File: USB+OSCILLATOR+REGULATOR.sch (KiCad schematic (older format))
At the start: 65 parts, among them J201 CONN_01X02, J202 USB_A, U201 MIC2005A-2, U202 74xx125, U203 93LCxxB_sot-23-6, U204 MIC5355/6-xYMME, U205 FT2232H

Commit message: Minor fixes and the gitignore was removed
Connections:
- net +5V: no longer R201.1, U201.3 (EN)
- net Vext_filtered: now also R201.1, U201.3 (EN)
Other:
- moved on the sheet: R201

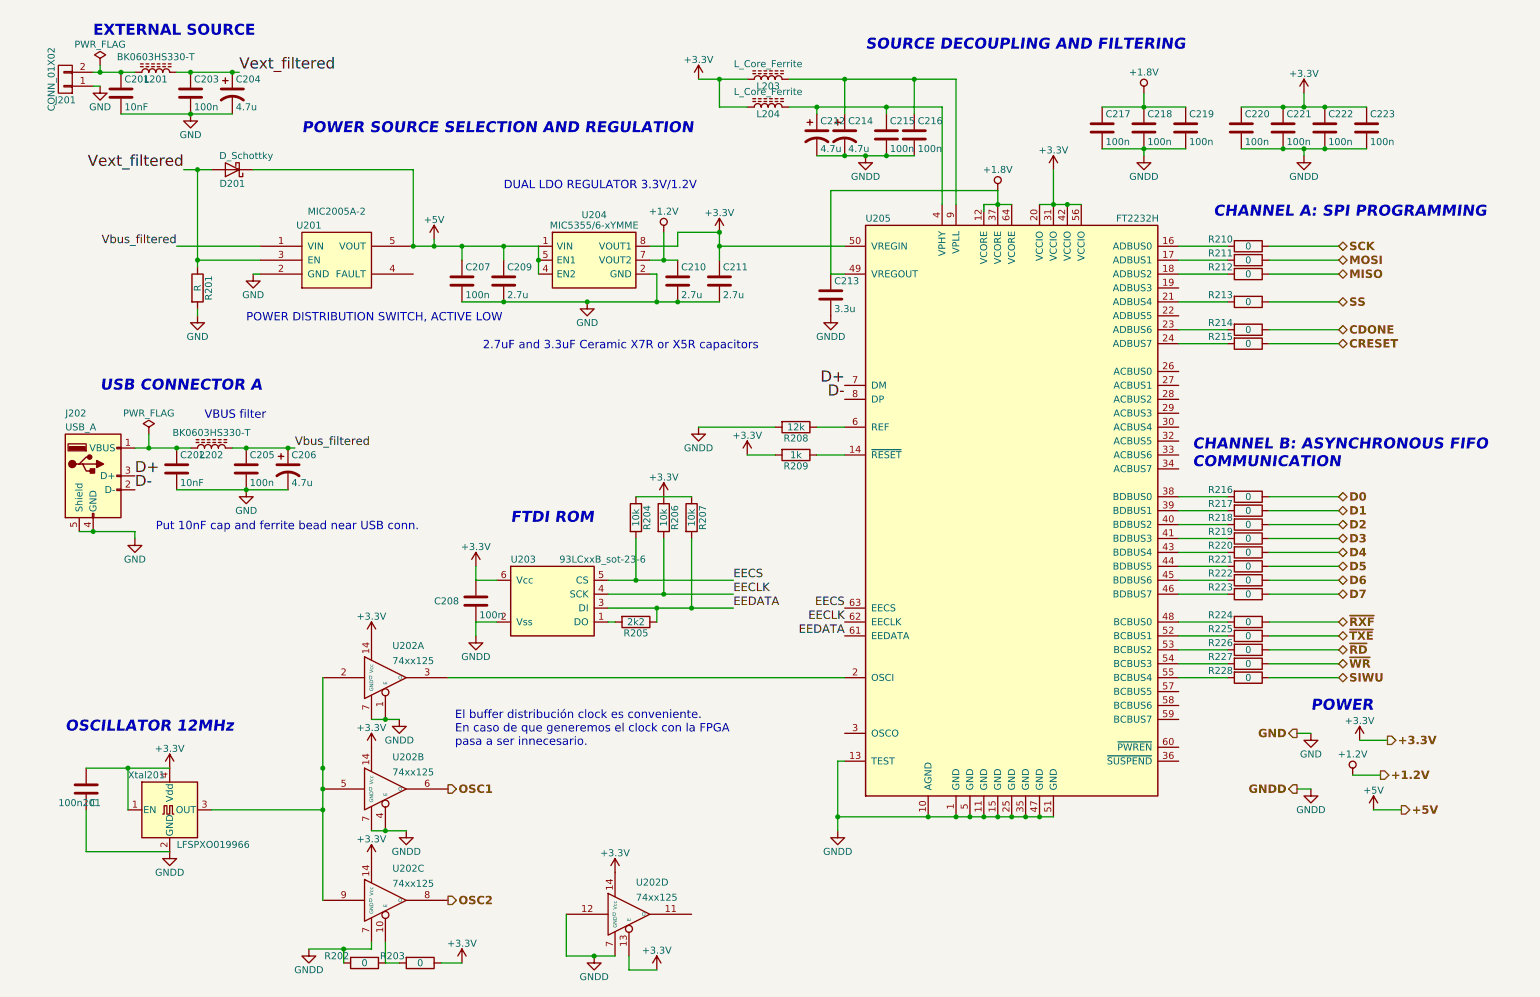
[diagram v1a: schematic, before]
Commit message: Added part numbers of sheet USB+...
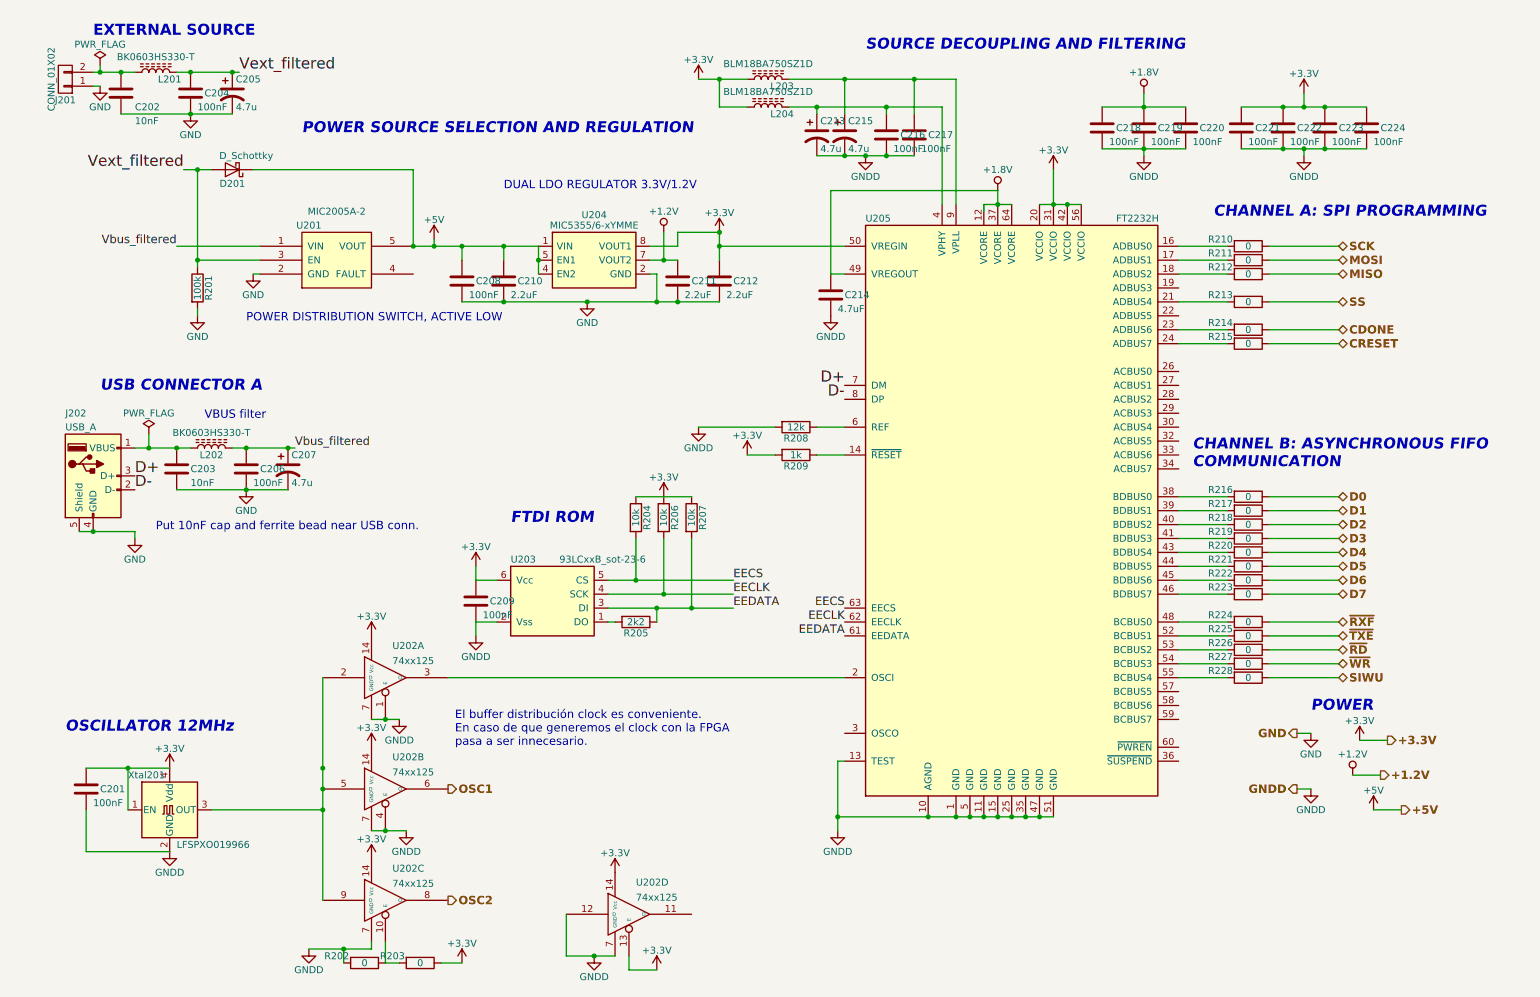
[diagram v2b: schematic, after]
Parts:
- removed 100n201: C, symbol C
- removed C202: 10nF, symbol C
- removed C204, C206, C214: 4.7u, symbol CP1
- removed C205, C207, C215: 100n, symbol C
- removed C213: 3.3u, symbol C
- added C201, C204, C206, C224: 100nF, Capacitors_SMD:C_0603_HandSoldering, symbol C
- added C205, C207, C215: 4.7u, symbol CP1
- added C212: 2.2uF, Capacitors_SMD:C_0805_HandSoldering, symbol C
- added C214: 4.7uF, Capacitors_SMD:C_0805_HandSoldering, symbol C
- C202: renamed from C201; footprint (none) -> Capacitors_SMD:C_0603_HandSoldering; Dielectric (none) -> X7R; Manufacturer Part (none) -> C0603C103K5RECTU; VDC (none) -> 25V (min. 10V)
- C203: value 100n -> 10nF; footprint (none) -> Capacitors_SMD:C_0603_HandSoldering; Dielectric (none) -> X7R; Manufacturer Part (none) -> C0603C103K5RECTU; VDC (none) -> 50V (min. 10V)
- C208, C216, C217, C218, C219, C220, C221, C222, C223: value 100n -> 100nF; footprint (none) -> Capacitors_SMD:C_0603_HandSoldering; Dielectric (none) -> X7R; Manufacturer Part (none) -> C0603C104K3RACTU; VDC (none) -> 25V (min. 10V)
- C209: value 2.7u -> 100nF; footprint (none) -> Capacitors_SMD:C_0603_HandSoldering; Dielectric (none) -> X7R; Manufacturer Part (none) -> C0603C104K3RACTU; VDC (none) -> 25V (min. 10V)
- C210, C211: value 2.7u -> 2.2uF; footprint (none) -> Capacitors_SMD:C_0805_HandSoldering; Dielectric (none) -> X7R; Manufacturer Part (none) -> GRM21BR71A225KA01K; VDC (none) -> 10V (min 10V)
- C213: renamed from C212; Datashet (none) -> http://www.mouser.com/ds/2/40/TAJ_AUTO-783622-1093304.pdf; Manufacturer Part (none) -> TAJA475K016UNJ; Type (none) -> Tantalum; VDC (none) -> 16V
- D201: footprint (none) -> Diodes_SMD:D_0603; Manufacturer Part Number (none) -> CDBURT0530LL-HF
- L201: footprint (none) -> Inductors_SMD:L_0603_HandSoldering; Impedance 100MHz (none) -> 120 (min 33); Manufacturer Part (none) -> BLM18AG121SN1D
- L203, L204: value L_Core_Ferrite -> BLM18BA750SZ1D; footprint (none) -> Inductors_SMD:L_0603_HandSoldering; Impedance 100MHz (none) -> 75; Manufacturer Part (none) -> BLM18AG121SN1D
- R201: value R -> 100k; footprint (none) -> Resistors_SMD:R_0603_HandSoldering; Manufacturer Part (none) -> RCA0603100KJNEC
- R202, R203, R210, R211, R212, R213, R214, R215, R216, R217, R218, R219, R220, R221, R222, R223, R224, R225, R226, R227, R228: footprint (none) -> Resistors_SMD:R_1206_HandSoldering; Current Max. (none) -> 2A; Manufacturer Part (none) -> RC1206JR-070RL
- R204, R206, R207: footprint (none) -> Resistors_SMD:R_0603_HandSoldering; Manufacterer Part (none) -> CRCW060310K0FKEA
- R205: footprint (none) -> Resistors_SMD:R_0603_HandSoldering; Manufacturer Part (none) -> CRCW06032K20FKEA
- R208: Manufacturer Part Number (none) -> 667-ERJ-1GEJ123C
- R209: Manufacturer part number (none) -> 667-ERJ-1GEJ102C
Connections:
- net +1.2V: now also C211.1; no longer C210.1
- net +1.8V: now also C220.1, C214.1; no longer C217.1
- net +3V3: now also C209.1, C201.1, C212.1, C224.1; no longer C208.1, C211.1, C220.1
- net +5V: now also C208.1, C210.1; no longer C209.1
- net GND: now also C208.2, C204.2, C205.2, C206.2, C207.2, C212.2; no longer C209.2
- net GNDD: now also C209.2, C201.2, C214.2, C215.2, C224.2; no longer C208.2
- net Vbus_filtered: now also C206.1, C207.1
- net Vext_filtered: now also C204.1, C205.1; no longer C203.1
- net at C213.1, L204.2, U205.4 (VPHY): now also C216.1
- net at L203.2, U205.9 (VPLL): now also C217.1, C215.1; no longer C216.1
- net at J202.1 (VBUS), L202.1: now also C203.1
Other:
- note removed: "2.7uF and 3.3uF Ceramic X7R or X5R capacitors"

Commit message: The schematic is now free of any ERC error. Not connected and power flags added. No more global power pins, hierarchical labels used for power connections. TODO list: -Check if all footpritns are already assigned. -Export a BOM list, and check if all part numbers are assigned. -Add leds and testpoints. -Make another branch, with the RAM connections to the left and right banks, so the ram could be located in the bottom layer and the FPGA in the top layer. -Reorder the connections of the current branch if necessary, do the placement of components and ground planes.
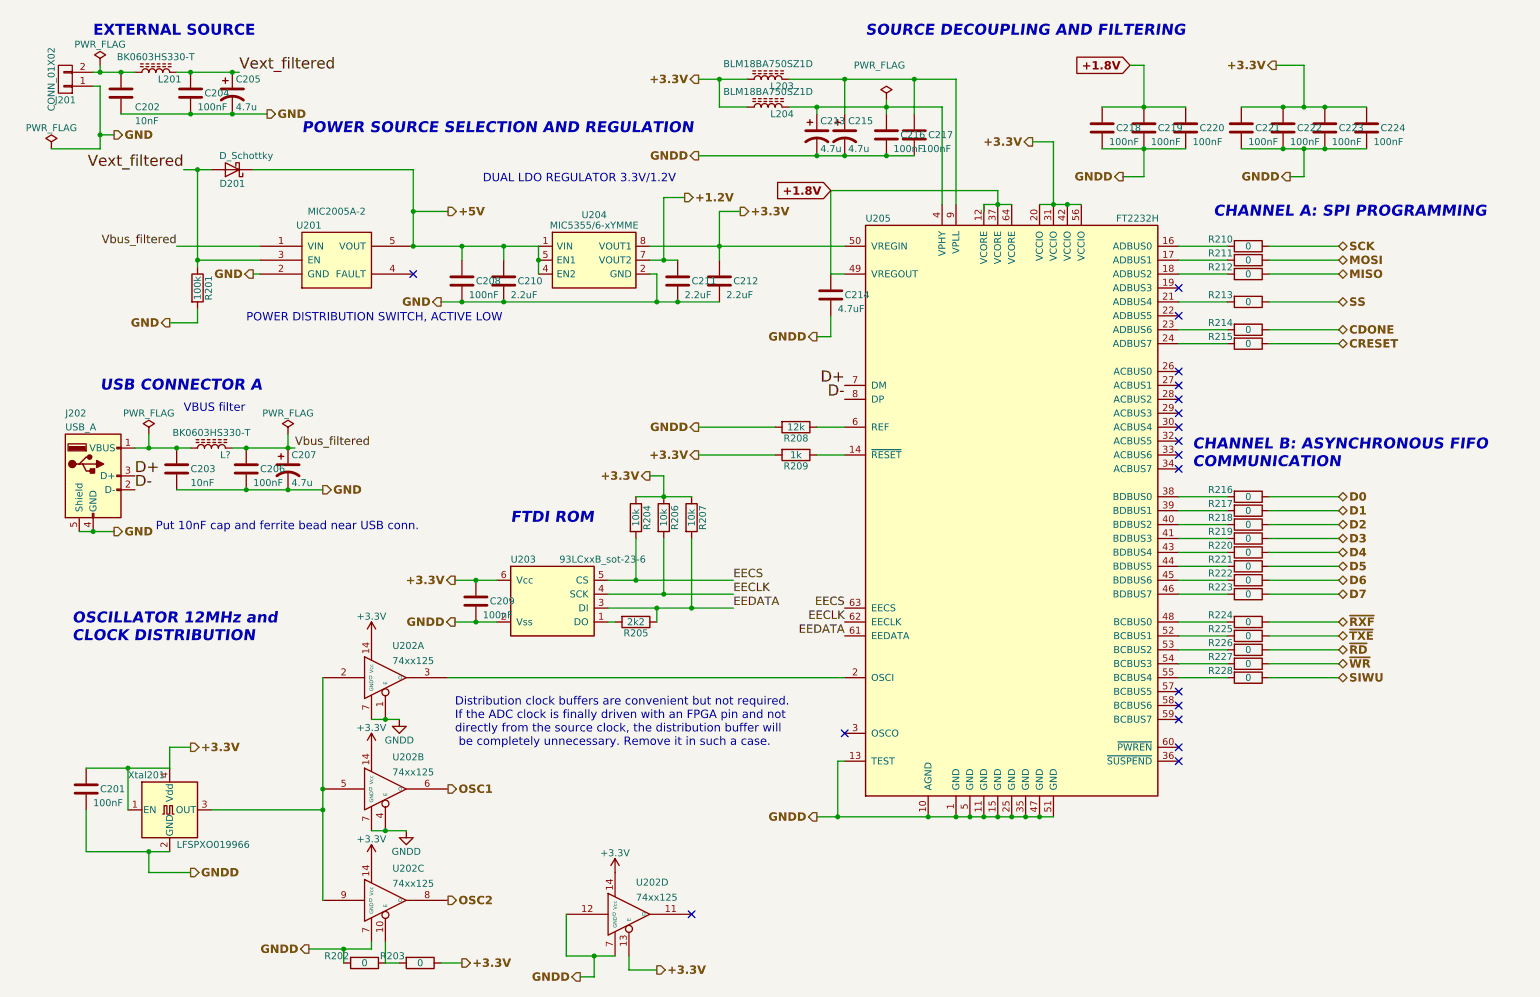
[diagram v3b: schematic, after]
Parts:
- removed L202: BK0603HS330-T, symbol L_Core_Ferrite
- added L?: BK0603HS330-T, Inductors_SMD:L_0603_HandSoldering, symbol L_Core_Ferrite
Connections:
- net +3V3: no longer C201.1, C209.1, C212.1, C221.1, C222.1, C223.1, C224.1, L203.1, L204.1, R203.1, R206.1, R209.2, U202.13 (E), U203.6 (Vcc), U204.8 (VOUT1), U205.20 (VCCIO), U205.31 (VCCIO), U205.42 (VCCIO), U205.50 (VREGIN), U205.56 (VCCIO), Xtal201.1 (EN), Xtal201.4 (Vdd)
- net Vbus_filtered: now also L?.2
- net +3.3V: now reaches R204.1, R207.1
- net +3.3V: now also C201.1, C209.1, C212.1, C221.1, C222.1, C223.1, C224.1, L203.1, L204.1, R203.1, R206.1, R209.2, U202.13 (E), U203.6 (Vcc), U204.8 (VOUT1), U205.20 (VCCIO), U205.31 (VCCIO), U205.42 (VCCIO), U205.50 (VREGIN), U205.56 (VCCIO), Xtal201.1 (EN), Xtal201.4 (Vdd)
- net at C203.1, J202.1 (VBUS): now also L?.1
- no-connect marks 0 -> 18
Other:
- note added: "Distribution clock buffers are convenient but not required.\nIf the ADC clock is finally driven with an FPGA pin and not \ndirectly from the source clock, the distribution buffer will\n be completely unnecessary. Remove it in such a case."
- note added: "OSCILLATOR 12MHz and \nCLOCK DISTRIBUTION"
- note removed: "El buffer distribución clock es conveniente.\nEn caso de que generemos el clock con la FPGA\npasa a ser innecesario.\n"
- note removed: "OSCILLATOR 12MHz\n"
- note removed: "POWER"

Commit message: First netlist export
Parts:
- removed J202: USB_A, symbol USB_A
- added J1: USB_OTG, Connectors:USB_Micro-B, symbol USB_OTG
- C205: footprint (none) -> Capacitors_SMD:CP_Elec_5x5.3
- C207, C213, C215: footprint (none) -> Capacitors_SMD:CP_Elec_5x5.7
- J201: footprint (none) -> Pin_Headers:Pin_Header_Angled_1x02_Pitch1.27mm
- R208, R209: footprint (none) -> Resistors_SMD:R_0603_HandSoldering
- R210, R211, R212, R213, R214, R215, R216, R217, R218, R219, R220, R221, R222, R223, R224, R225, R226, R227, R228: footprint Resistors_SMD:R_1206_HandSoldering -> Resistors_SMD:R_0603_HandSoldering
- U201: footprint MODULE -> TO_SOT_Packages_SMD:SOT-23-5_HandSoldering
- U202: footprint (none) -> Housings_SSOP:SSOP-14_5.3x6.2mm_Pitch0.65mm
- U203: footprint (none) -> TO_SOT_Packages_SMD:SOT-23-6_Handsoldering
- U204: footprint (none) -> TO_SOT_Packages_SMD:SOT-23-6
- U205: footprint (none) -> Housings_QFP:LQFP-64_10x10mm_Pitch0.5mm
- gave numbers to parts that had none: 1
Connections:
- no-connect marks 18 -> 19

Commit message: Added three indicator LEDs. Two green leds, one indicating if usb power is connected, and the other one indicating if the external power source is connected. One red led indicating if fault condition happens in MIC2005A-2
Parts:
- added D? (x3): LED_ALT, LEDs:LED_0603, symbol LED_ALT
- added R? (x3): 1500, Resistors_SMD:R_0603_HandSoldering, symbol R
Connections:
- wire segments 155 -> 162
- no-connect marks 19 -> 18
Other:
- note added: "POWER DISTRIBUTION \nSWITCH, ACTIVE LOW"
- note removed: "POWER DISTRIBUTION SWITCH, ACTIVE LOW"

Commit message: Fist approach of board placement
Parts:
- added D205: GREEN, LEDs:LED_0603, symbol LED_ALT
- added D206: YELLOW, LEDs:LED_0603, symbol LED_ALT
- added D207: RED, LEDs:LED_0603, symbol LED_ALT
- added R232, R233, R234: 680, Resistors_SMD:R_0603_HandSoldering, symbol R
- D203: renamed from D?; value LED_ALT -> RED
- D204: renamed from D?; value LED_ALT -> GREEN
- U204: footprint TO_SOT_Packages_SMD:SOT-23-6 -> TO_SOT_Packages_SMD:SOT-23-8_Handsoldering
- gave numbers to parts that had none: 4
- renumbered J1 to J202, L1 to L202, R202 to R203, R203 to R206, R204 to R207, R205 to R208, R206 to R209, R207 to R210, R208 to R211, R209 to R212, R210 to R213, R211 to R214, R212 to R215, R213 to R216, R214 to R217, R215 to R218, R216 to R219, R217 to R220, R218 to R221, R219 to R222, R220 to R223, R221 to R224, R222 to R225, R223 to R226, R224 to R227, R225 to R228, R226 to R229, R227 to R230, R228 to R231
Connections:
- wire segments 162 -> 172
- no-connect marks 18 -> 15

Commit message: Clk's buffers were removed and pcb routing was started
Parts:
- removed R203, R206: 0, Resistors_SMD:R_1206_HandSoldering, symbol R
- removed U202: 74xx125, Housings_SSOP:SSOP-14_5.3x6.2mm_Pitch0.65mm, symbol 74xx125
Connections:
- net labels removed: OSC1, OSC2
- wire segments 172 -> 158
- no-connect marks 15 -> 14
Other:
- note removed: "Distribution clock buffers are convenient but not required.\nIf the ADC clock is finally driven with an FPGA pin and not \ndirectly from the source clock, the distribution buffer will\n be completely unnecessary. Remove it in such a case."
- moved on the sheet: C201, Xtal201

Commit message: Placing de algunos capas de acople y otras giladas
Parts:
- C213, C215: footprint Capacitors_SMD:CP_Elec_5x5.7 -> Capacitors_SMD:C_1206_HandSoldering
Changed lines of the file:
@@
 F 0 "C213" H 6425 1550 50  0000 L CNN
 F 1 "4.7u" H 6425 1350 50  0000 L CNN
-F 2 "Capacitors_SMD:CP_Elec_5x5.7" H 6400 1450 50  0001 C CNN
+F 2 "Capacitors_SMD:C_1206_HandSoldering" H 6400 1450 50  0001 C CNN
 F 3 "" H 6400 1450 50  0001 C CNN
 F 4 "TAJA475K016UNJ" H 6400 1450 60  0001 C CNN "Manufacturer Part"
@@
 F 0 "C215" H 6625 1550 50  0000 L CNN
 F 1 "4.7u" H 6625 1350 50  0000 L CNN
-F 2 "Capacitors_SMD:CP_Elec_5x5.7" H 6600 1450 50  0001 C CNN
+F 2 "Capacitors_SMD:C_1206_HandSoldering" H 6600 1450 50  0001 C CNN
 F 3 "" H 6600 1450 50  0001 C CNN
 F 4 "TAJA475K016UNJ" H 6600 1450 60  0001 C CNN "Manufacturer Part"
